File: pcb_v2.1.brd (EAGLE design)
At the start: 19.4 x 108.4 mm, 57 parts, among them J1 PJ301_THONKICONN6, J2 PJ301_THONKICONN6, J3 PJ301_THONKICONN6, J4 PJ301_THONKICONN6, U1 MCP6004, U2 TL074_SMD, U5 TL074

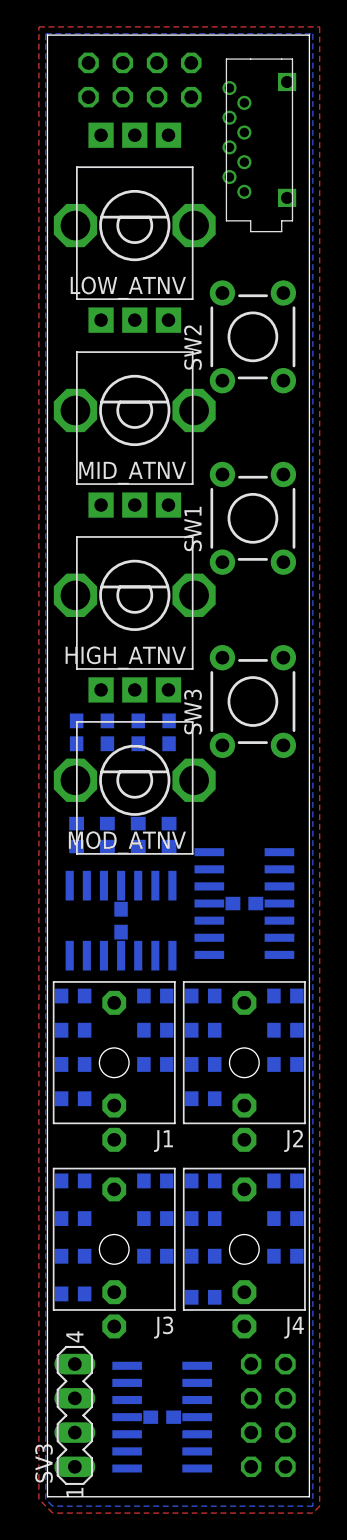
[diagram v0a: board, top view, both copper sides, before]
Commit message: place v2 components
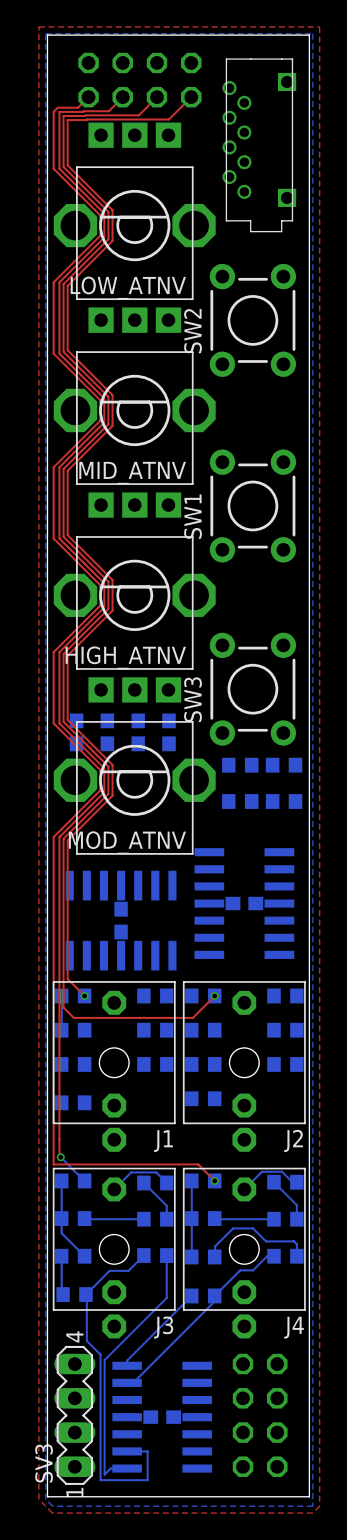
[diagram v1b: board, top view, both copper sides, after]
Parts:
- moved R5 12.4 mm to (14.9, 51.3), turned to 0 degrees
- moved R11 11.1 mm to (14.9, 53.9), turned to 0 degrees
- moved R17 11.1 mm to (18.2, 51.3), turned to 0 degrees
- moved R24 10.5 mm to (12.2, 14.6)
- moved R35 10.5 mm to (18.3, 23.0)
- moved R13 10.3 mm to (2.64, 14.7), turned to 180 degrees
- moved R27 10.2 mm to (8.64, 23.0)
- moved R23 9.98 mm to (18.2, 53.9), turned to 0 degrees
- moved R30 7.92 mm to (2.54, 28.9)
- moved R3 7.62 mm to (2.54, 36.8)
- moved R32 7.62 mm to (12.2, 29.2)
- moved R9 7.62 mm to (12.2, 36.8)
- moved R22 6.73 mm to (12.2, 17.5), turned to 180 degrees
- moved R34 6.68 mm to (18.3, 20.3)
- moved R20 6.68 mm to (8.64, 20.3)
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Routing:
- net MOD_IN: track 0.00 -> 105.0 mm, vias 0 -> 1
- net MID_IN: track 0.00 -> 96.9 mm, vias 0 -> 1
- net HIGH_IN: track 0.00 -> 96.3 mm, vias 0 -> 1
- net LOW_IN: track 0.00 -> 86.4 mm, vias 0 -> 1
- net N$23: track 0.00 -> 26.9 mm
- net N$27: track 0.00 -> 20.0 mm
- net N$24: track 0.00 -> 15.0 mm
- net N$19: track 0.00 -> 8.86 mm
- net N$28: track 0.00 -> 7.17 mm
- net N$37: track 0.00 -> 6.29 mm
- net N$38: track 0.00 -> 5.64 mm
- net N$35: track 0.00 -> 4.76 mm
- net N$12: track 0.00 -> 4.74 mm
- net N$13: track 0.00 -> 4.42 mm
- net N$36: track 0.00 -> 4.42 mm
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
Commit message: new board layout
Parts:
- moved R29 8.00 mm to (8.64, 36.9), turned to 180 degrees
- moved R31 8.00 mm to (18.3, 36.9), turned to 180 degrees
- moved R1 7.81 mm to (2.54, 32.0), turned to 180 degrees
- moved R12 6.68 mm to (12.2, 29.0)
- moved R7 6.62 mm to (12.2, 34.2)
- moved R10 6.62 mm to (12.2, 31.7)
- moved R32 6.57 mm to (18.3, 31.6)
- moved R26 6.10 mm to (18.3, 34.3)
- moved R30 0.61 mm to (2.54, 29.5)
- moved R3 0.30 mm to (2.84, 36.8)
- turned R16 to 180 degrees
- turned R2 to 180 degrees
- turned R6 to 180 degrees
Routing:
- net N$14: track 2.89 -> 43.0 mm, vias 0 -> 2
- net N$8: track 0.00 -> 32.5 mm, vias 0 -> 4
- net N$37: track 6.29 -> 32.7 mm, vias 0 -> 4
- net N$9: track 0.00 -> 24.2 mm, vias 0 -> 2
- net N$33: track 0.00 -> 20.0 mm, vias 0 -> 2
- net N$3: track 0.00 -> 19.5 mm
- net N$31: track 2.54 -> 21.6 mm
- net N$2: track 0.00 -> 15.6 mm
- net N$4: track 0.00 -> 13.2 mm, vias 0 -> 2
- net N$1: track 0.00 -> 10.9 mm
- net N$22: track 0.00 -> 6.76 mm
- net N$20: track 0.00 -> 6.69 mm
- net N$32: track 0.00 -> 2.45 mm
- net N$30: track 0.00 -> 2.45 mm
- net MID_IN: track 96.9 -> 97.5 mm, vias 1 -> 3
